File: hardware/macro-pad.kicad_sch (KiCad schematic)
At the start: 41 parts, among them J1 USB_C_Receptacle_USB2.0, SW1 PEC12R-4025F-S0024, SW2 MX1A-G1NA, SW3 MX1A-G1NA, SW4 MX1A-G1NA, SW5 MX1A-G1NA, U1 MIC5317-3.3ZD5-TR, U2 RP2040, U3 W25Q128JVSIQ, Y1 ABLS-12.000MHZ-B4-T

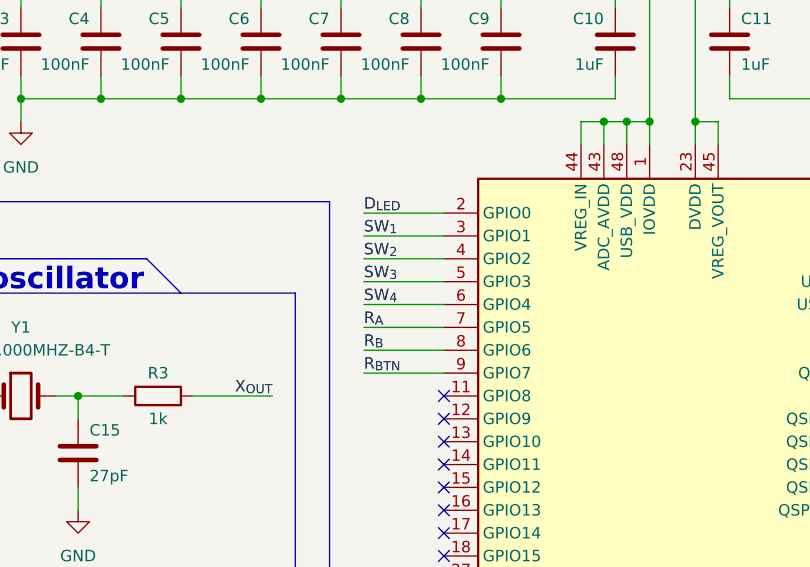
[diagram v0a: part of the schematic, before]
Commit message: Rearranged micocontroller pins for easier routing
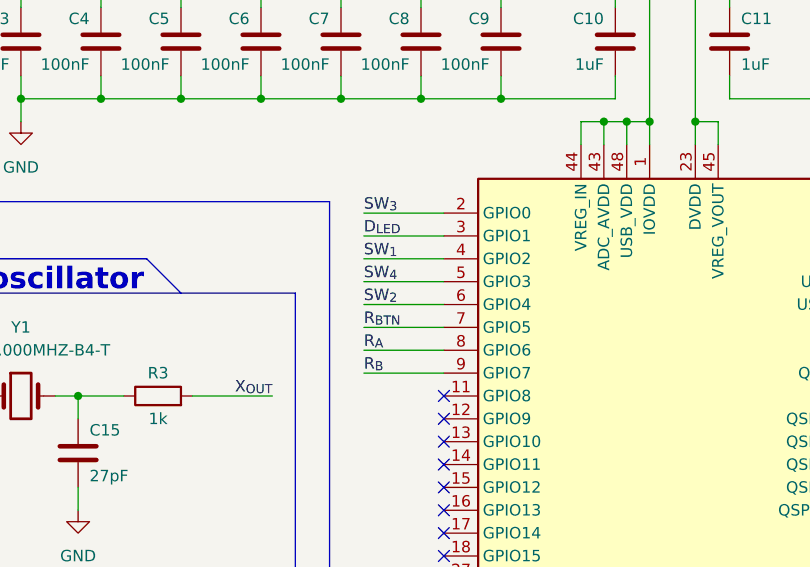
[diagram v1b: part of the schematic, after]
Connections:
- net D_{LED}: now also U2.3 (GPIO1); no longer U2.2 (GPIO0)
- net R_{A}: now also U2.8 (GPIO6); no longer U2.7 (GPIO5)
- net R_{BTN}: now also U2.7 (GPIO5); no longer U2.9 (GPIO7)
- net R_{B}: now also U2.9 (GPIO7); no longer U2.8 (GPIO6)
- net SW_{1}: now also U2.4 (GPIO2); no longer U2.3 (GPIO1)
- net SW_{2}: now also U2.6 (GPIO4); no longer U2.4 (GPIO2)
- net SW_{3}: now also U2.2 (GPIO0); no longer U2.5 (GPIO3)
- net SW_{4}: now also U2.5 (GPIO3); no longer U2.6 (GPIO4)
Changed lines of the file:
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@@
     (effects (font (size 1.27 1.27)) (justify right bottom))
   )
-  (label "R_{B}" (at 171.45 77.47 0)
+  (label "R_{B}" (at 171.45 80.01 0)
     (effects (font (size 1.27 1.27)) (justify left bottom))
   )
@@
     (effects (font (size 1.27 1.27)) (justify right bottom))
   )
-  (label "R_{BTN}" (at 171.45 80.01 0)
+  (label "R_{BTN}" (at 171.45 74.93 0)
     (effects (font (size 1.27 1.27)) (justify left bottom))
   )
-  (label "SW_{4}" (at 171.45 72.39 0)
+  (label "SW_{4}" (at 171.45 69.85 0)
     (effects (font (size 1.27 1.27)) (justify left bottom))
   )
@@
     (effects (font (size 1.27 1.27)) (justify left bottom))
   )
-  (label "SW_{2}" (at 171.45 67.31 0)
+  (label "SW_{2}" (at 171.45 72.39 0)
     (effects (font (size 1.27 1.27)) (justify left bottom))
   )
@@
     (effects (font (size 1.27 1.27)) (justify right bottom))
   )
-  (label "SW_{3}" (at 171.45 69.85 0)
+  (label "SW_{3}" (at 171.45 62.23 0)
     (effects (font (size 1.27 1.27)) (justify left bottom))
   )
-  (label "D_{LED}" (at 171.45 62.23 0)
+  (label "D_{LED}" (at 171.45 64.77 0)
     (effects (font (size 1.27 1.27)) (justify left bottom))
   )
@@
     (effects (font (size 1.27 1.27)) (justify left bottom))
   )
-  (label "R_{A}" (at 171.45 74.93 0)
+  (label "R_{A}" (at 171.45 77.47 0)
     (effects (font (size 1.27 1.27)) (justify left bottom))
   )
@@
     (effects (font (size 1.27 1.27)) (justify right bottom))
   )
-  (label "SW_{1}" (at 171.45 64.77 0)
+  (label "SW_{1}" (at 171.45 67.31 0)
     (effects (font (size 1.27 1.27)) (justify left bottom))
   )
